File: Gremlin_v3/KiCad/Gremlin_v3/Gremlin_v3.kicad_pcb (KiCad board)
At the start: 2 copper layers, 92 x 112.8 mm, 49 parts, among them J1 JST_02, J2 Conn_01x05, SW1 Switch, SW2 SW_SPST, U1 Nice_Nano_V2

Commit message: pcb updates
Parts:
- added G***: LOGO, LOGO, F.Cu at (140.0, 120.5)
- J2: value Conn_01x05 -> 5034800540; footprint Connector_FFC-FPC:Amphenol_F32Q-1A7x1-11005_1x05-1MP_P0.5mm_Horizontal -> Molex ZIF Connector:CONN_503480-0540_MOL
- moved J2 404.4 mm to (188.7, 132.6)
- moved D1 404.3 mm to (113.9, 63.1)
- moved D10 404.3 mm to (185.9, 80.1)
- moved D11 404.3 mm to (113.9, 97.1)
- moved D12 404.3 mm to (131.9, 92.1)
- moved D13 404.3 mm to (149.9, 87.1)
- moved D14 404.3 mm to (167.9, 92.1)
- moved D15 404.3 mm to (185.9, 97.1)
- moved D16 404.3 mm to (113.9, 114.1)
- moved D17 404.3 mm to (131.9, 109.1)
- moved D18 404.3 mm to (149.9, 104.1)
- moved D19 404.3 mm to (167.9, 109.1)
- moved D2 404.3 mm to (131.9, 58.1)
- moved D20 404.3 mm to (185.9, 114.1)
- moved D21 404.3 mm to (159.9, 130.6)
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- renumbered D26 to D21, D27 to D22, S26 to S21, S27 to S22
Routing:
- net Col 2: track 170.0 -> 167.5 mm
- net Net-(J2-Pin_5): track 101.8 -> 104.0 mm
- net Col 4: track 133.2 -> 131.5 mm
- net Row 4: track 51.7 -> 53.3 mm
- net Net-(SW2-A): track 31.0 -> 29.5 mm
- net Col 3: track 145.8 -> 144.4 mm
- net Net-(J1-Pad2): track 40.5 -> 39.3 mm
- net Net-(J2-Pin_1): track 80.7 -> 81.9 mm
- net Net-(J2-Pin_4): track 75.9 -> 77.1 mm
- net Net-(J2-Pin_2): track 83.3 -> 84.6 mm
- net Net-(J2-Pin_3): track 78.1 -> 79.4 mm
- net Row 0: track 163.0 -> 163.7 mm
- net Col 1: track 119.0 -> 118.4 mm
- net Col 0: track 95.4 -> 94.7 mm
- net Row 2: track 133.3 -> 132.7 mm

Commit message: pcb design updates
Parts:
- added ?: , , F.Cu at (135.2, 62.2)
- added ?: , , F.Cu at (117.2, 67.0)
- added ?: , , F.Cu at (171.2, 73.2)
- added REF**: MountingHole_2.2mm_M2_DIN965_Pad, MountingHole:MountingHole_2.2mm_M2_DIN965_Pad, F.Cu at (146.8, 136.0)
- added REF**: MountingHole_2.2mm_M2_DIN965_Pad, MountingHole:MountingHole_2.2mm_M2_DIN965_Pad, F.Cu at (187.0, 122.5)
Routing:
- net Col 3: track 144.4 -> 147.9 mm
- net Col 4: track 131.5 -> 130.7 mm
- added copper zone on B.Cu, net (none)
- added copper zone on F.Cu, net (none)

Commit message: Updated PCB design for CNC Milling
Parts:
- moved D21 4.37 mm to (164.2, 131.4), turned to 85 degrees
- moved D22 3.27 mm to (174.9, 133.8), turned to 35 degrees
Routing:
- net Row 4: track 53.3 -> 48.2 mm
- net Net-(D22-A): track 8.53 -> 10.9 mm
- net Net-(D21-A): track 8.83 -> 6.64 mm
- net Col 3: track 147.9 -> 149.1 mm

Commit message: udpated pcb for cnc
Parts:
- removed ? (x3): , 
- removed REF** (x2): MountingHole_2.2mm_M2_DIN965_Pad, MountingHole:MountingHole_2.2mm_M2_DIN965_Pad
- moved SW2 5.60 mm to (111.3, 148.6)
- moved SW1 5.25 mm to (103.4, 145.3), turned to -90 degrees
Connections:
- J2 pad 5: Net-(J2-Pin_5) -> GND
- SW1 pad 1: Net-(J2-Pin_5) -> GND
- U1 pad 3: Net-(J2-Pin_5) -> unconnected-(U1-GND-Pad3)
- U1 pad 4: unconnected-(U1-GND-Pad4) -> GND
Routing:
- net Net-(J2-Pin_5): track 104.0 -> 0.00 mm, vias 2 -> 0
- net Net-(U1-RST): track 29.9 -> 40.4 mm
- net Net-(SW2-A): track 29.8 -> 35.1 mm
- net GND: track 0.00 -> 5.25 mm
- net Col 3: track 149.1 -> 153.9 mm
- net Col 4: track 130.7 -> 135.0 mm
- net Net-(SW2-B): track 29.5 -> 32.2 mm
- net Col 2: track 167.5 -> 165.2 mm
- net Col 0: track 94.7 -> 96.1 mm
- net Net-(J2-Pin_1): track 81.9 -> 80.6 mm
- net Row 4: track 48.2 -> 46.9 mm
- net Net-(J2-Pin_2): track 84.6 -> 83.4 mm
- net Net-(J2-Pin_3): track 79.5 -> 78.6 mm
- net Net-(J1-Pad2): track 39.3 -> 38.5 mm
- net unconnected-(U1-GND-Pad3): track 0.00 -> 0.69 mm
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- added copper zone on B.Cu, net GND
- added copper zone on F.Cu, net GND
- removed copper zone on B.Cu, net (none)
- removed copper zone on F.Cu, net (none)

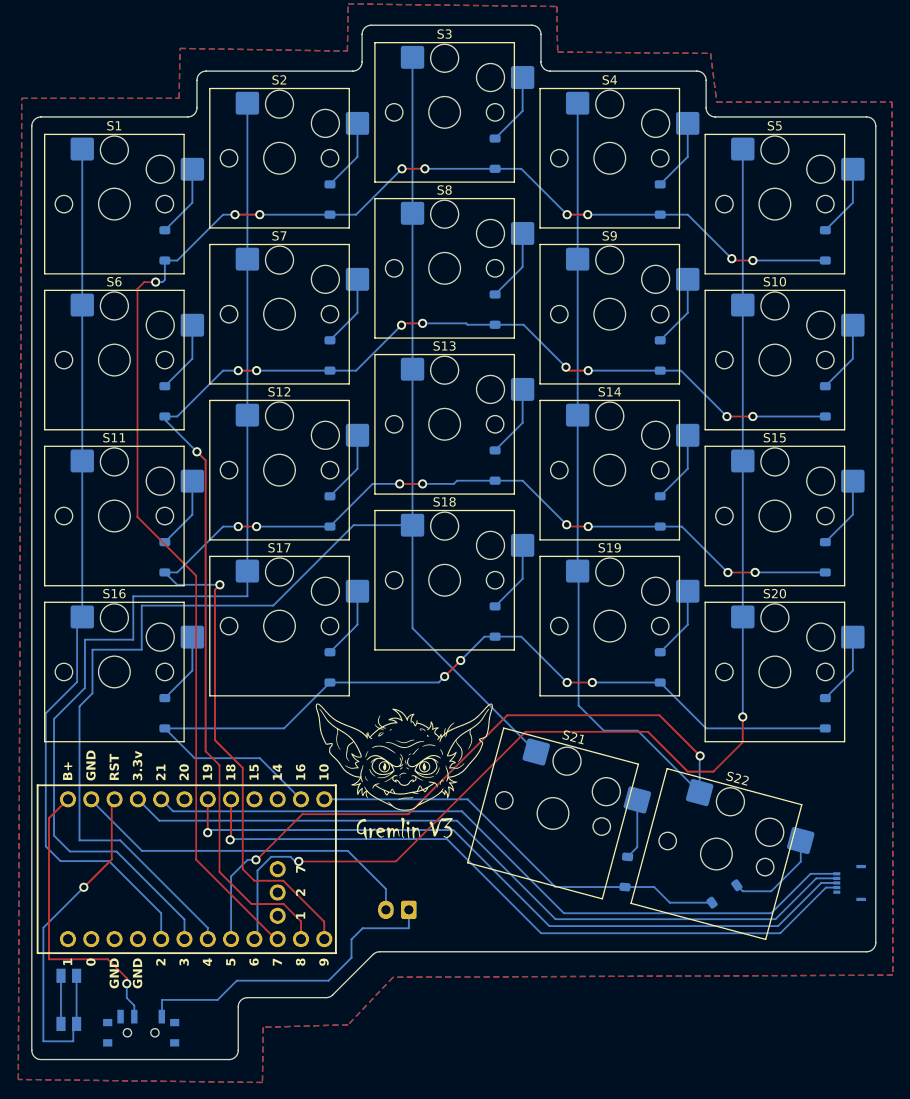
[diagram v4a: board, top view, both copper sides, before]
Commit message: updated PCB for better trace creation using a cnc
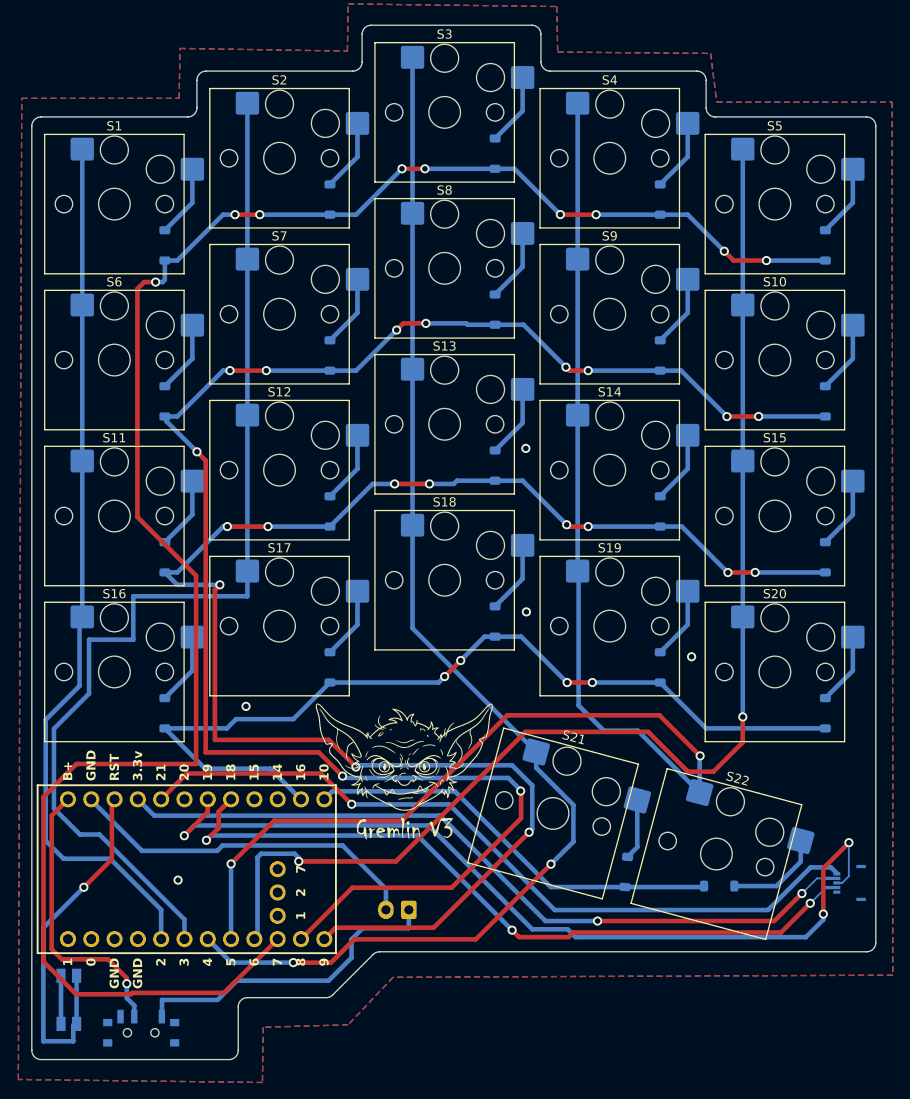
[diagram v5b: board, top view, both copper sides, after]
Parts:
- moved D22 1.03 mm to (174.3, 132.9), turned to 0 degrees
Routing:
- net Row 0: track 163.1 -> 206.0 mm
- net Row 1: track 145.6 -> 187.5 mm, vias 9 -> 11
- net Row 2: track 132.5 -> 173.2 mm, vias 9 -> 11
- net Col 2: track 165.2 -> 139.1 mm, vias 0 -> 2
- net Net-(J2-Pin_3): track 78.6 -> 95.8 mm, vias 1 -> 3
- net Net-(J2-Pin_4): track 76.8 -> 81.0 mm, vias 1 -> 3
- net Net-(J2-Pin_1): track 80.6 -> 83.2 mm, vias 0 -> 1
- net Col 1: track 119.1 -> 117.1 mm
- net Col 4: track 135.0 -> 136.3 mm
- net Net-(SW2-B): track 32.2 -> 31.1 mm
- net Row 4: track 46.9 -> 46.0 mm
- net Col 3: track 153.9 -> 154.7 mm
- net Net-(J2-Pin_2): track 83.4 -> 83.3 mm, vias 0 -> 2
- net GND: vias 0 -> 5
